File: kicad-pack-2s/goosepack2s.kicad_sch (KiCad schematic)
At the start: 67 parts, among them J1 USB_C_Receptacle_USB2.0_16P, J11 Balance 2S, J2 Pack lead, J3 XT30UPB-M, Q2 IRF8736, Q3 IRF8736, Q4 AO3400A, Q5 AO3400A, U13 S-8252AAH, U21 HY2213-BB3A, U22 HY2213-BB3A, U7 BQ25798

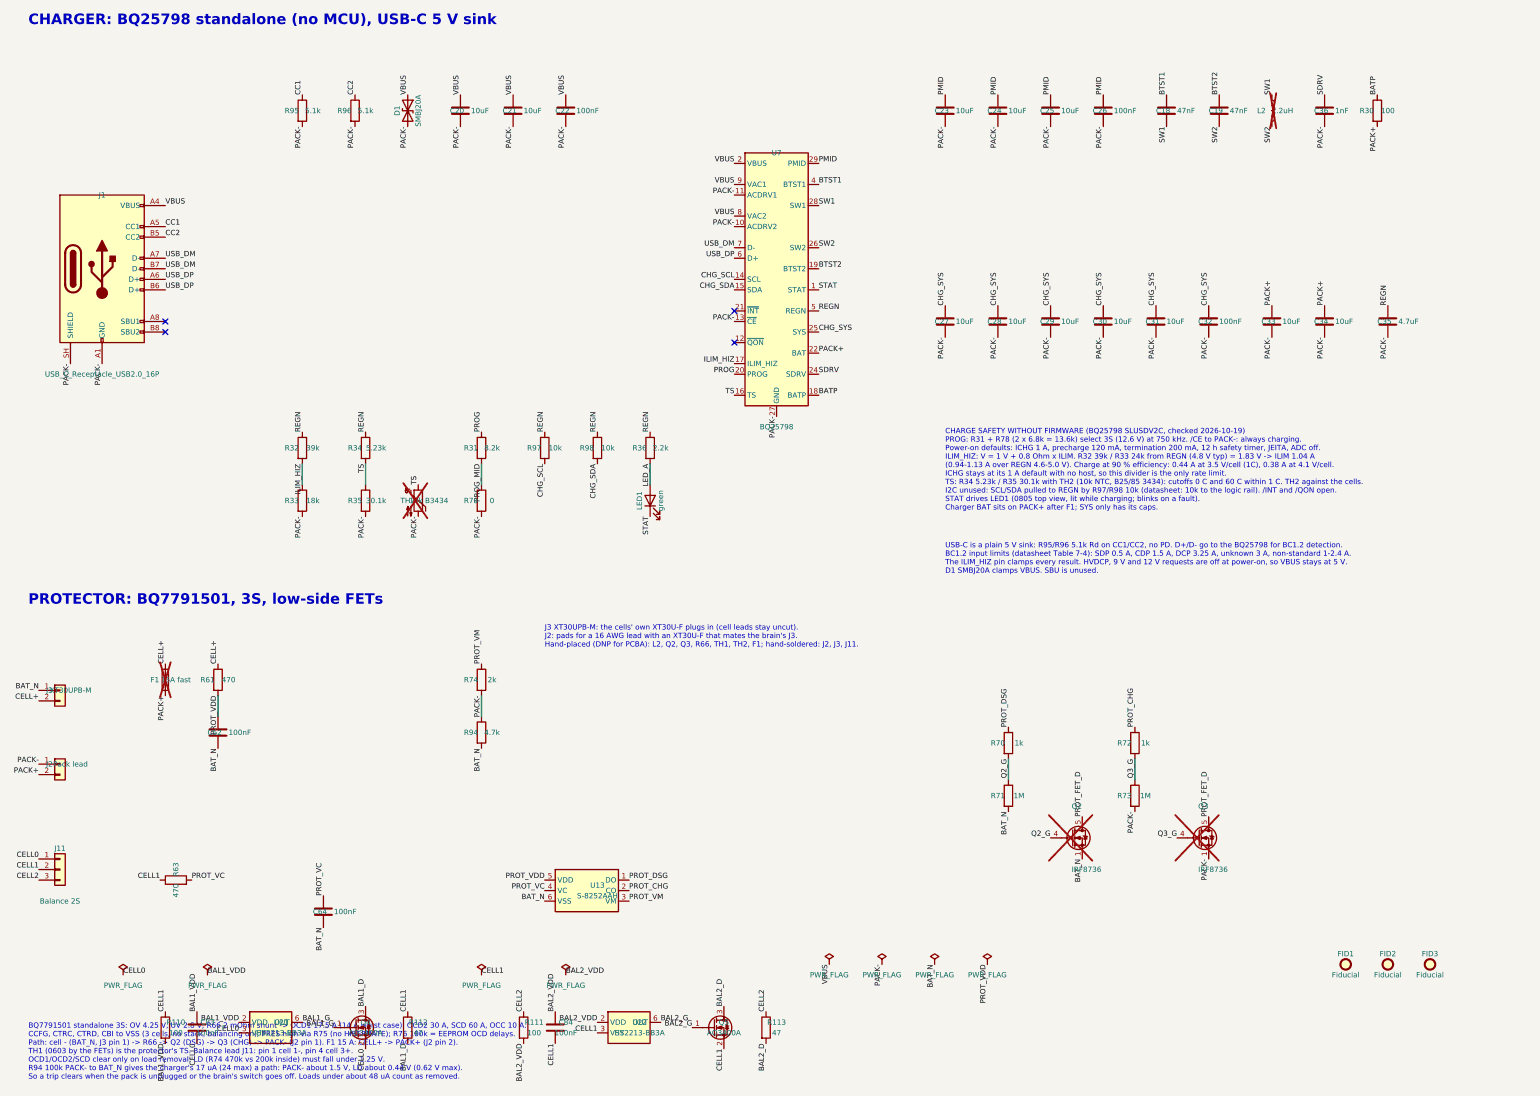
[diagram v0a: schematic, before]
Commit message: Fill in LCSC numbers, swap to stocked parts, tidy the new schematic parts
- LCSC numbers from JLC's 2026-10-19 in-stock catalog for every new part
  except the DRV8251A, which JLC doesn't stock (Global Sourcing or consign).
- 2S protector S-8252AAH -> HY2120-LB (C168778): pin-for-pin the same,
  OV 4.25 V / UV 2.80 V, stocked at JLC. R94 trip recovery still holds.
- IPROPI R101-R106 1.18k (2,341 in stock) -> 1.2k preferred (C25862),
  so the motor limit is 1.34 A.
- Fix the 2S pack board's footprint-symbol links (paths were dropped in
  the previous commit); both boards now link every footprint correctly.
- Move the VREF divider and the balancer block into clear space and
  rewrite the stale DRV8871/BQ7791501 notes on the motor and 2S sheets.

Co-Authored-By: Claude Opus 5.5 <noreply@anthropic.com>
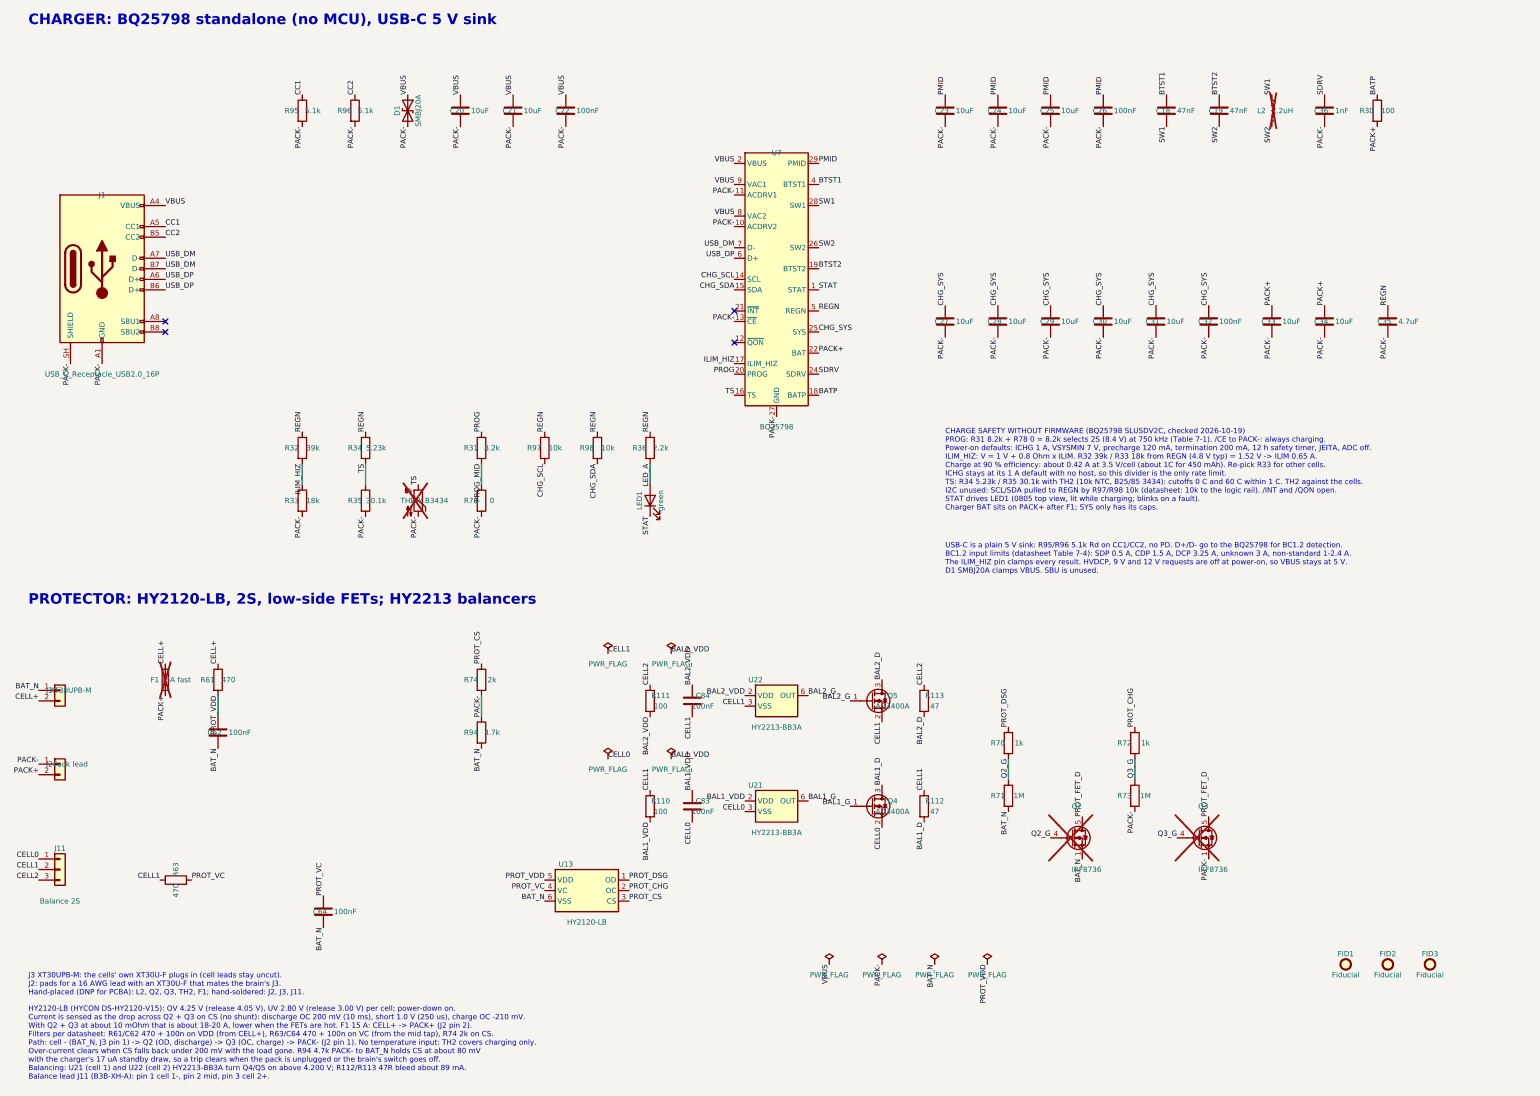
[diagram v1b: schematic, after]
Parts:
- J11: LCSC Part # (none) -> C144394
- R112, R113: LCSC Part # (none) -> C15261
- R31: LCSC Part # (none) -> C25924
- R33: LCSC Part # (none) -> C25762
- R61, R63: LCSC Part # (none) -> C25117
- R74: LCSC Part # (none) -> C4109
- R78: LCSC Part # (none) -> C17168
- U13: value S-8252AAH -> HY2120-LB; symbol hexyhustle:S8252 -> hexyhustle:HY2120; LCSC Part # (none) -> C168778; MPN S-8252AAH-M6T1U -> HY2120-LB; Manufacturer ABLIC -> HYCON
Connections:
- net PROT_VM renamed PROT_CS
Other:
- note added: "CHARGE SAFETY WITHOUT FIRMWARE (BQ25798 SLUSDV2C, checked 2026-10-19) PROG: R31 8.2k + R78 0 = 8.2k selects 2S (8.4 V) at 750 kHz (Table 7-1). /CE to PACK-: always charging. Power-on defaults: ICHG 1 A, VSYSMIN 7 V, precharge 120 mA, termination 200 mA, 12 h safety timer, JEITA, ADC off. ILIM_HIZ: V = 1 V + 0.8 Ohm x ILIM. R32 39k / R33 18k from REGN (4.8 V typ) = 1.52 V -> ILIM 0.65 A. Charge at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"
- note added: "HY2120-LB (HYCON DS-HY2120-V15): OV 4.25 V (release 4.05 V), UV 2.80 V (release 3.00 V) per cell; power-down on. Current is sensed as the drop across Q2 + Q3 on CS (no shunt): discharge OC 200 mV (10 ms), short 1.0 V (250 us), charge OC -210 mV. With Q2 + Q3 at about 10 mOhm that is about 18-20 A, lower when the FETs are hot. F1 15 A: CELL+ -> PACK+ (J2 pin 2). Filters per datasheet: R61/C62 470 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"
- note added: "J3 XT30UPB-M: the cells' own XT30U-F plugs in (cell leads stay uncut). J2: pads for a 16 AWG lead with an XT30U-F that mates the brain's J3. Hand-placed (DNP for PCBA): L2, Q2, Q3, TH2, F1; hand-soldered: J2, J3, J11."
- note added: "PROTECTOR: HY2120-LB, 2S, low-side FETs; HY2213 balancers"
- note removed: "BQ7791501 standalone 3S: OV 4.25 V, UV 2.8 V; R66 2 mOhm shunt -> OCD1 17.5 A (14 A worst case), OCD2 30 A, SCD 60 A, OCC 10 A. CCFG, CTRC, CTRD, CBI to VSS (3 cells, no stack, balancing on); PRES high via R75 (no HIBERNATE); R76 100k = EEPROM OCD delays. Path: cell - (BAT_N, J3 pin 1) -> R66 -> Q2 (DSG) -> Q3 (CHG) -> PACK- (J2 pin 1). F1 15 A: CELL+ -> PACK+ (J2 pin 2). TH1 (0603 by the FETs) i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"
- note removed: "CHARGE SAFETY WITHOUT FIRMWARE (BQ25798 SLUSDV2C, checked 2026-10-19) PROG: R31 + R78 (2 x 6.8k = 13.6k) select 3S (12.6 V) at 750 kHz. /CE to PACK-: always charging. Power-on defaults: ICHG 1 A, precharge 120 mA, termination 200 mA, 12 h safety timer, JEITA, ADC off. ILIM_HIZ: V = 1 V + 0.8 Ohm x ILIM. R32 39k / R33 24k from REGN (4.8 V typ) = 1.83 V -> ILIM 1.04 A (0.94-1.13 A over REGN 4.6-5.0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"
- note removed: "J3 XT30UPB-M: the cells' own XT30U-F plugs in (cell leads stay uncut). J2: pads for a 16 AWG lead with an XT30U-F that mates the brain's J3. Hand-placed (DNP for PCBA): L2, Q2, Q3, R66, TH1, TH2, F1; hand-soldered: J2, J3, J11."
- note removed: "PROTECTOR: BQ7791501, 3S, low-side FETs"
- moved on the sheet: C83, C84, Q4, Q5, R110, R111, R112, R113, U21, U22
